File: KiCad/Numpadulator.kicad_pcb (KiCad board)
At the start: 2 copper layers, 3.4 x 3 mm, 58 parts, among them SW1 Cherry_MX_RGB_WS2812, SW10 Cherry_MX_RGB_WS2812, SW11 Cherry_MX_RGB_WS2812, SW12 Cherry_MX_RGB_WS2812, SW13 Cherry_MX_RGB_WS2812, SW14 Cherry_MX_RGB_WS2812, SW15 Cherry_MX_RGB_WS2812, SW16 Cherry_MX_RGB_WS2812, SW17 Cherry_MX_RGB_WS2812, SW18 Cherry_MX_RGB_WS2812, SW19 Rotary_Encoder_Switch, SW2 Cherry_MX_RGB_WS2812, SW3 Cherry_MX_RGB_WS2812, SW4 Cherry_MX_RGB_WS2812, SW5 Cherry_MX_RGB_WS2812, SW6 Cherry_MX_RGB_WS2812, SW7 Cherry_MX_RGB_WS2812, SW8 Cherry_MX_RGB_WS2812, SW9 Cherry_MX_RGB_WS2812, U1 PRO_MICRO_C, U2 OLED_SSD1306

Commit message: More layout and frustration 3:
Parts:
- removed SW17, SW18, SW6: Cherry_MX_RGB_WS2812, Cherry MX:Cherry-MX_PCB-Mounted_LTST-A683CEGBW_Kailh_Socket
- added D20: WS2816, Custom-parts:SK6812-MINI-E, F.Cu at (73.0, 165.1)
- added D21: WS2816, Custom-parts:SK6812-MINI-E, F.Cu at (115.9, 112.7)
- added D22: WS2816, Custom-parts:SK6812-MINI-E, F.Cu at (115.9, 150.8)
- added MX1: MX-NoLED, MX_Only:MXOnly-2U-Hotswap, F.Cu at (73.0, 160.3)
- added MX2: MX-NoLED, MX_Only:MXOnly-2U-Hotswap, F.Cu at (120.7, 112.7)
- added MX3: MX-NoLED, MX_Only:MXOnly-2U-Hotswap, F.Cu at (120.7, 150.8)
- SW1, SW10, SW11, SW12, SW13, SW14, SW15, SW16, SW2, SW3, SW4, SW5, SW7, SW8, SW9: footprint Cherry MX:Cherry-MX_PCB-Mounted_LTST-A683CEGBW_Kailh_Socket -> Custom-parts:Cherry-MX_PCB-Mounted_SK6812-MINI-E_Kailh_Socket
- moved U2 67.0 mm to (83.3, 38.1)
- moved U1 62.6 mm to (114.3, 64.3), turned to 90 degrees

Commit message: Laid out PCB
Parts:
- C1, C10, C11, C12, C13, C14, C15, C16, C17, C18, C2, C3, C4, C5, C6, C7, C8, C9, D12, D14, D15, D16, D17, D18, D19, D5, D6, D7: moved to B.Cu
- moved C6 224.1 mm to (65.9, 165.1), turned to 270 degrees
- moved D5 222.3 mm to (71.4, 141.3), turned to 90 degrees
- moved D6 214.2 mm to (81.0, 160.3), turned to 90 degrees
- moved D15 187.2 mm to (109.5, 160.3), turned to 90 degrees
- moved D14 185.6 mm to (109.5, 141.3), turned to 90 degrees
- moved D7 184.9 mm to (90.5, 84.1), turned to 90 degrees
- moved D12 172.4 mm to (109.5, 103.2), turned to 90 degrees
- moved D17 168.1 mm to (120.7, 142.9), turned to 180 degrees
- moved D18 162.3 mm to (120.7, 104.8), turned to 180 degrees
- moved D16 160.4 mm to (120.7, 55.6)
- moved C7 147.0 mm to (75.4, 88.9), turned to 270 degrees
- moved D19 146.0 mm to (128.6, 84.1), turned to 90 degrees
- moved C8 136.5 mm to (75.4, 108.0), turned to 270 degrees
- moved SW19 132.2 mm to (120.7, 65.1)
- moved C9 128.2 mm to (75.4, 127.0), turned to 270 degrees
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
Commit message: Better PCB layout
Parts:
- moved D1 57.2 mm to (71.4, 46.0)
- moved SW1 57.2 mm to (63.5, 46.0)
- moved C1 56.4 mm to (57.1, 50.8)
- moved D19 39.9 mm to (116.7, 46.0)
- moved D16 29.7 mm to (128.6, 84.1), turned to 90 degrees
- moved U2 22.2 mm to (83.3, 39.7)
- moved U1 19.1 mm to (113.5, 65.1), turned to 90 degrees
- moved SW19 19.1 mm to (120.7, 46.0), turned to 90 degrees

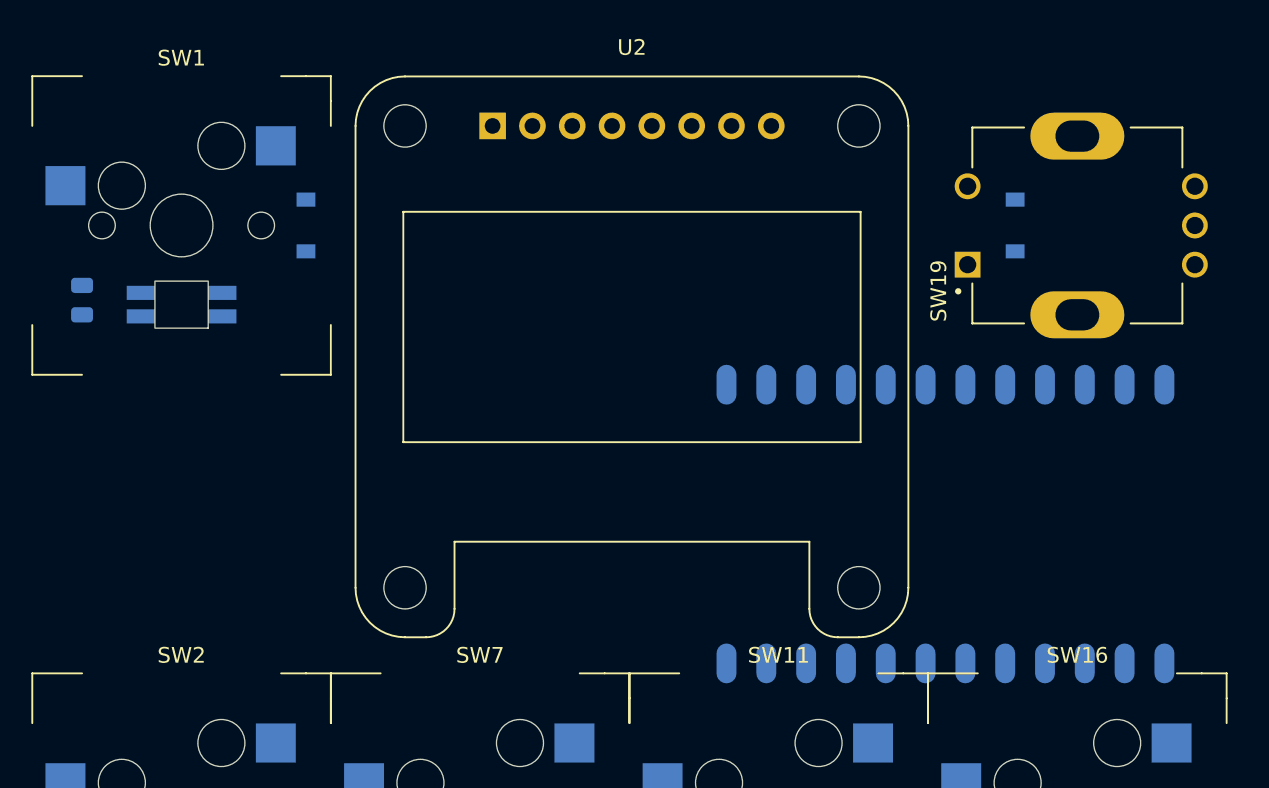
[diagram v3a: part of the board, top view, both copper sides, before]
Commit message: Moved MCU via the Genius of WIll
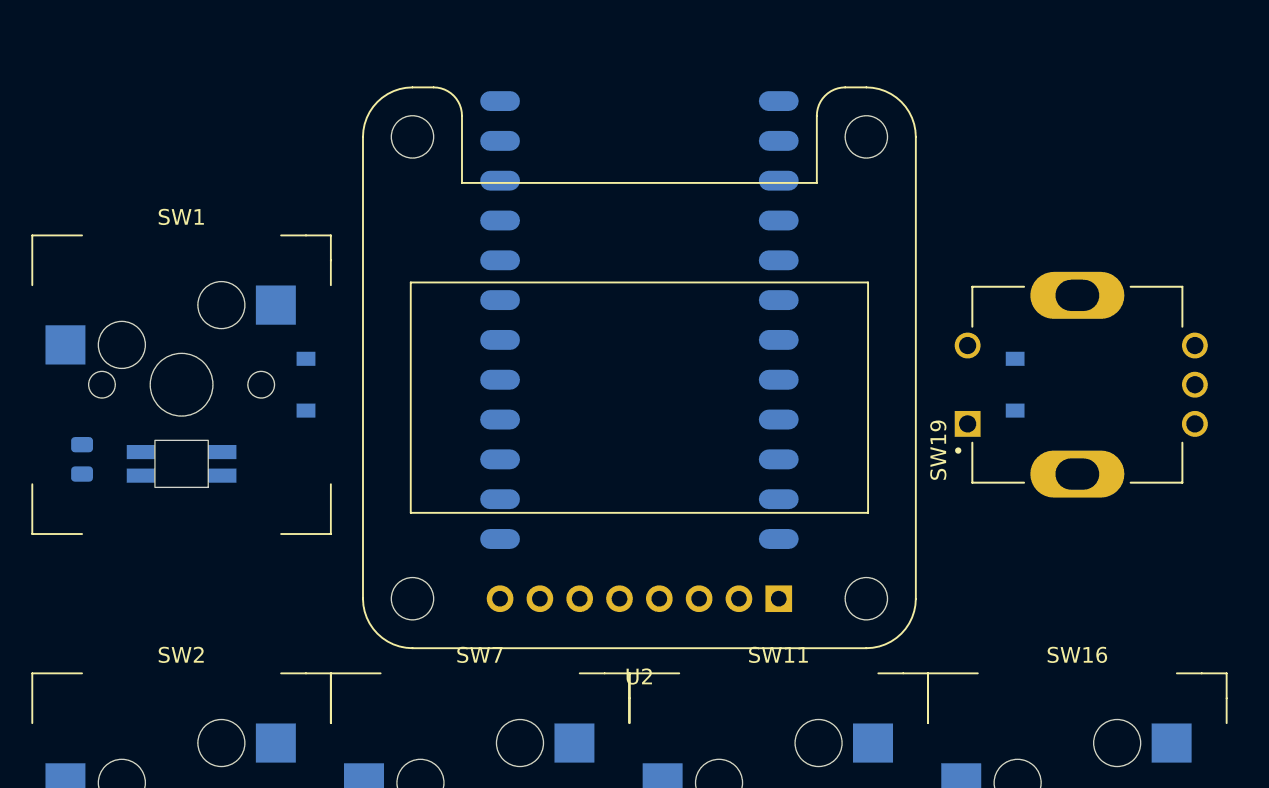
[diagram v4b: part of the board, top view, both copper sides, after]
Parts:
- moved U2 35.3 mm to (101.6, 69.8), turned to 180 degrees
- moved U1 25.2 mm to (92.7, 50.8), turned to 180 degrees
- moved C1 10.2 mm to (57.1, 61.0)
- moved D1 10.2 mm to (71.4, 56.2)
- moved D19 10.2 mm to (116.7, 56.2)
- moved SW1 10.2 mm to (63.5, 56.2)
- moved SW19 10.2 mm to (120.7, 56.2)

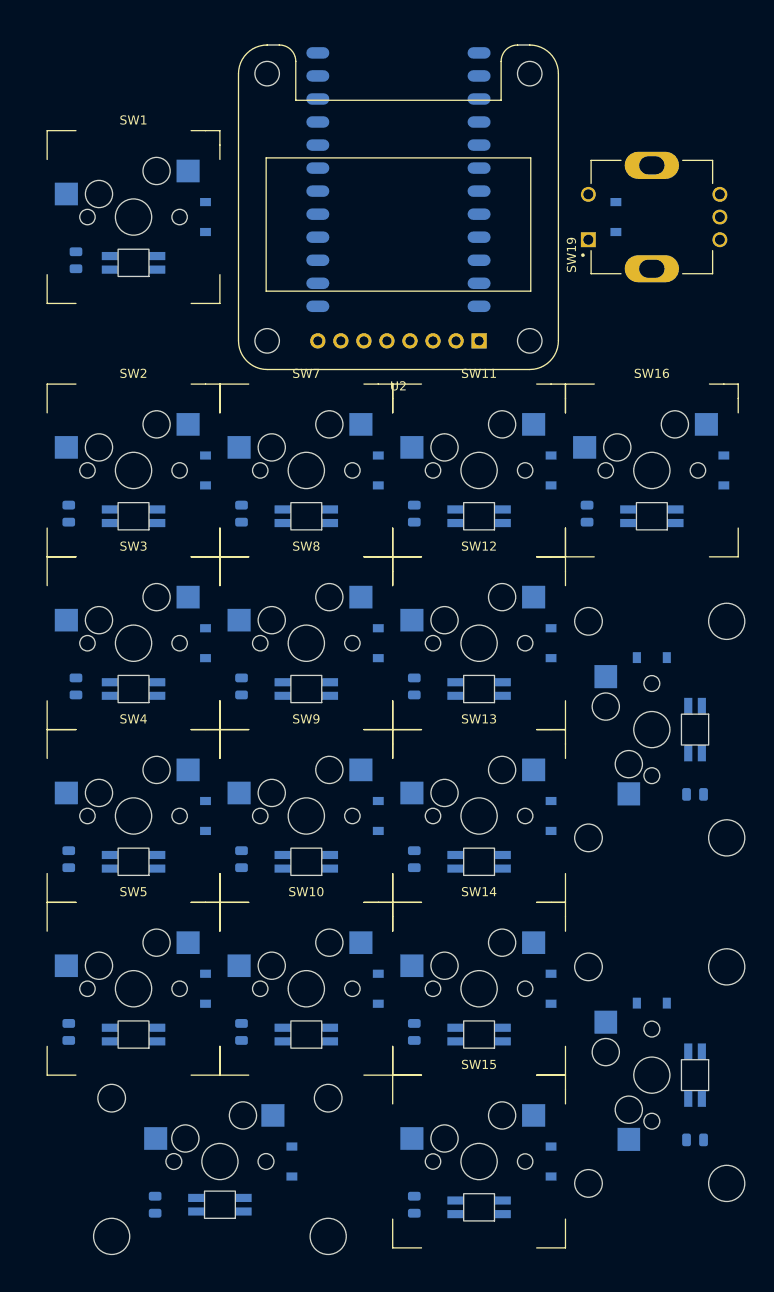
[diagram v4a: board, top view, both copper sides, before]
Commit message: Traced edge cuts
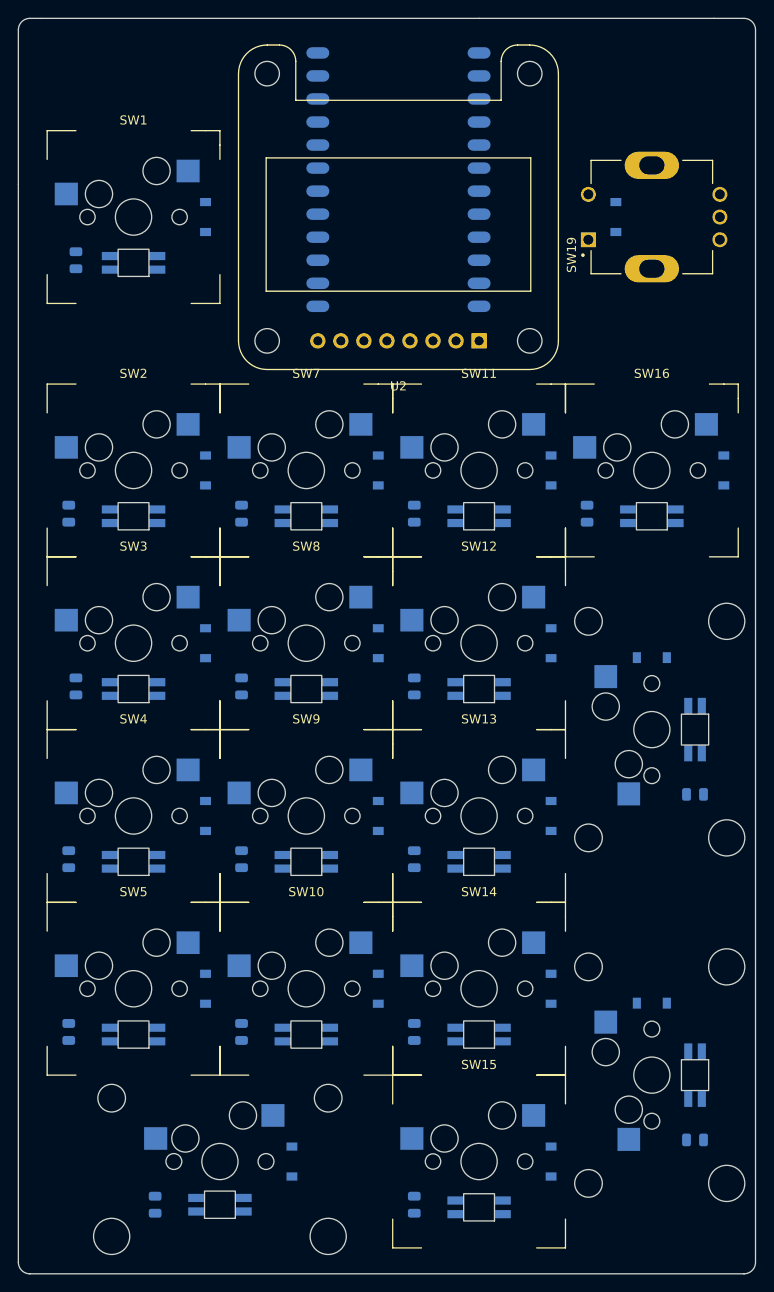
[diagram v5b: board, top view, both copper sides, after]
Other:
- board size 3.4 x 3 mm -> 81.3 x 138.4 mm

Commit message: add some power to the caps
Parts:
- moved C15 0.51 mm to (94.5, 165.6)
- moved C1 0.51 mm to (57.1, 61.5)
- moved C11 0.51 mm to (94.5, 89.4)
- moved C12 0.51 mm to (94.5, 108.5)
- moved C13 0.51 mm to (94.5, 127.5)
- moved C16 0.51 mm to (113.5, 89.4)
- moved C2 0.51 mm to (56.4, 89.4)
- moved C3 0.51 mm to (57.1, 108.5)
- moved C4 0.51 mm to (56.4, 127.5)
- moved C7 0.51 mm to (75.4, 89.4)
- moved C8 0.51 mm to (75.4, 108.5)
- moved C9 0.51 mm to (75.4, 127.5)
- moved C10 0.51 mm to (75.4, 146.6)
- moved C14 0.51 mm to (94.5, 146.6)
- moved C5 0.51 mm to (56.4, 146.6)
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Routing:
- net VCC: track 0.00 -> 560.2 mm, vias 0 -> 7
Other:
- net class Default: trace_width 0.25 -> 0.254
- net class Power added: clearance 0.2, trace_width 0.381, via_dia 0.8, via_drill 0.4

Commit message: started some LED routing
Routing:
- net LED: track 0.00 -> 60.2 mm, vias 0 -> 2

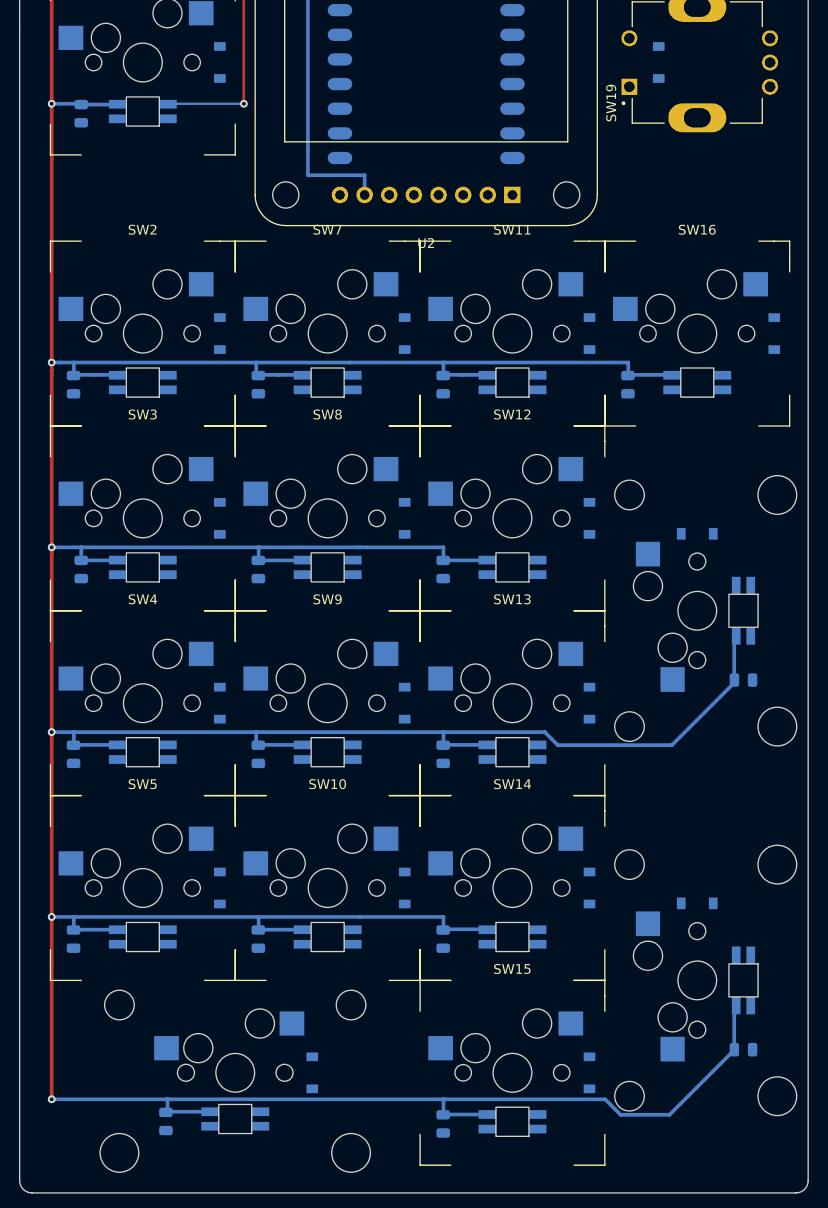
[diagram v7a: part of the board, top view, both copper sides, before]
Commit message: added some whack wiring for LEDs and some Columns
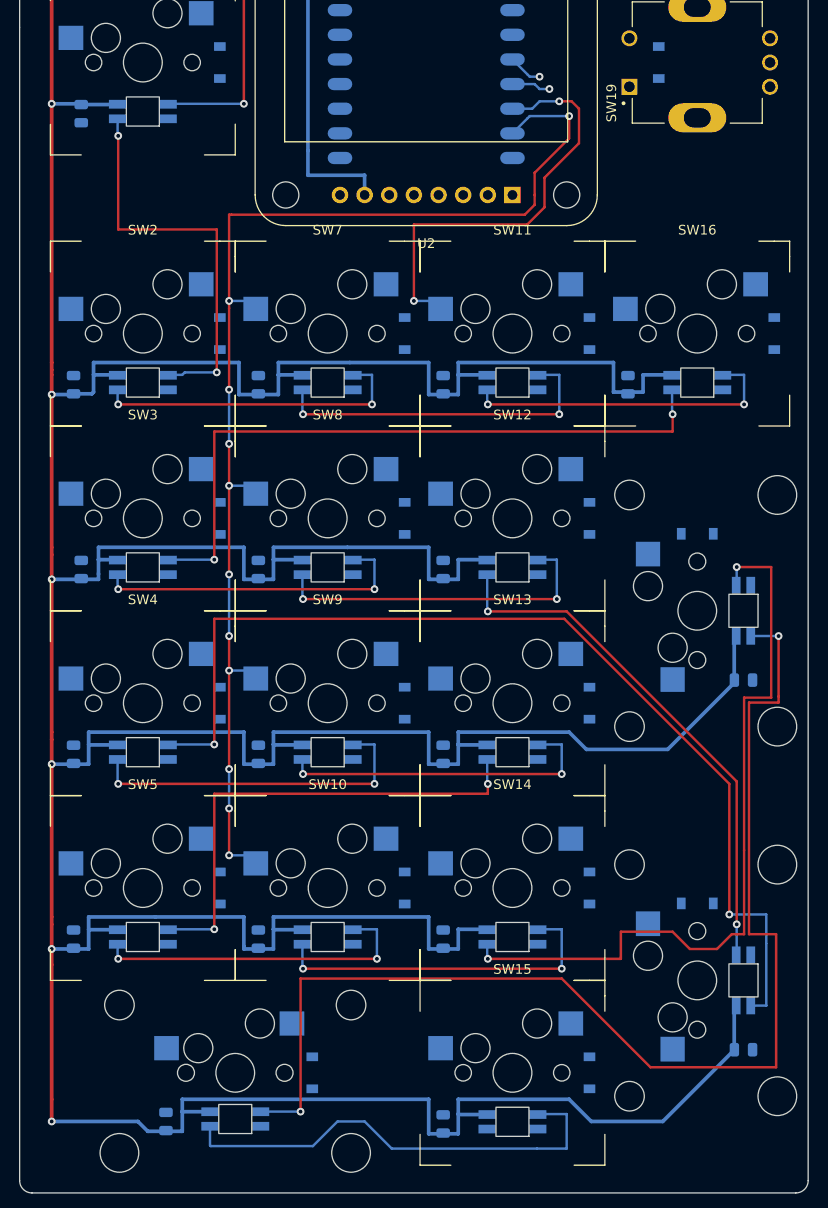
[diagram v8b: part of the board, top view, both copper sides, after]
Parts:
- turned C10 to 90 degrees
- turned C11 to 90 degrees
- turned C12 to 90 degrees
- turned C13 to 90 degrees
- turned C14 to 90 degrees
- turned C15 to 90 degrees
- turned C16 to 90 degrees
- turned C2 to 90 degrees
- turned C3 to 90 degrees
- turned C4 to 90 degrees
- turned C5 to 90 degrees
- turned C6 to 90 degrees
- turned C7 to 90 degrees
- turned C8 to 90 degrees
- turned C9 to 90 degrees
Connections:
- U1 pad 11: COL3 -> COL1
- U1 pad 9: COL1 -> COL3
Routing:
- net COL1: track 0.00 -> 124.5 mm, vias 0 -> 11
- net Net-(D20-Pad4): track 0.00 -> 123.8 mm, vias 0 -> 2
- net Net-(D21-Pad2): track 0.00 -> 105.9 mm, vias 0 -> 2
- net Net-(D22-Pad4): track 0.00 -> 78.1 mm, vias 0 -> 2
- net Net-(SW16-Pad2): track 0.00 -> 69.1 mm, vias 0 -> 2
- net Net-(D21-Pad4): track 0.00 -> 54.8 mm, vias 0 -> 2
- net Net-(SW13-Pad2): track 0.00 -> 50.3 mm, vias 0 -> 2
- net Net-(D20-Pad2): track 0.00 -> 47.1 mm
- net VCC: track 560.2 -> 607.2 mm
- net COL2: track 0.00 -> 43.5 mm, vias 0 -> 2
- net Net-(SW1-Pad2): track 0.00 -> 41.5 mm, vias 0 -> 2
- net Net-(SW10-Pad2): track 0.00 -> 36.1 mm, vias 0 -> 2
- net Net-(SW4-Pad2): track 0.00 -> 34.8 mm, vias 0 -> 2
- net Net-(SW11-Pad4): track 0.00 -> 34.8 mm, vias 0 -> 2
- net Net-(SW12-Pad4): track 0.00 -> 34.3 mm, vias 0 -> 2
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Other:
- board text added: "This wiring is bad and I should feel bad"
